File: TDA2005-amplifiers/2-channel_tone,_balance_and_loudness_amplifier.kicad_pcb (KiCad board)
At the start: 2 copper layers, 38 parts, among them U1 TDA2005

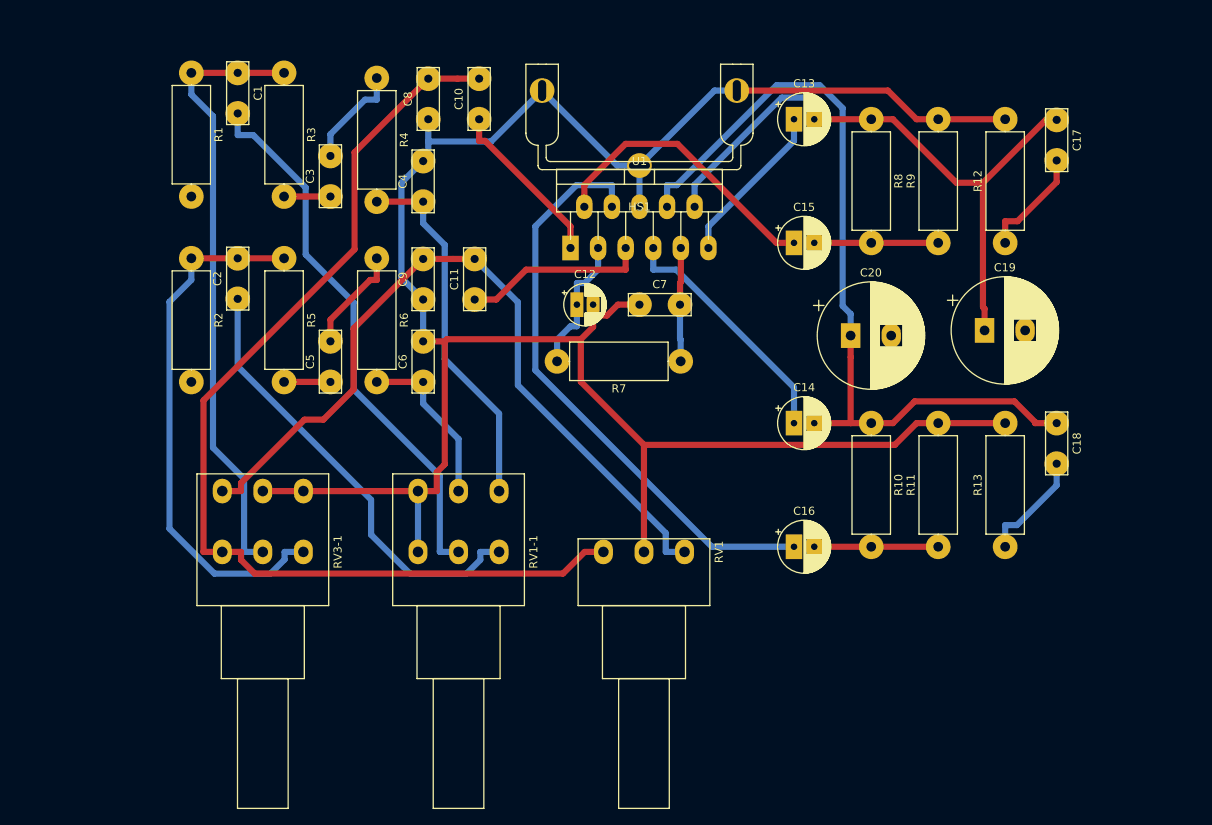
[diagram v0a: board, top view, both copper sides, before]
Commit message: new potentiometers
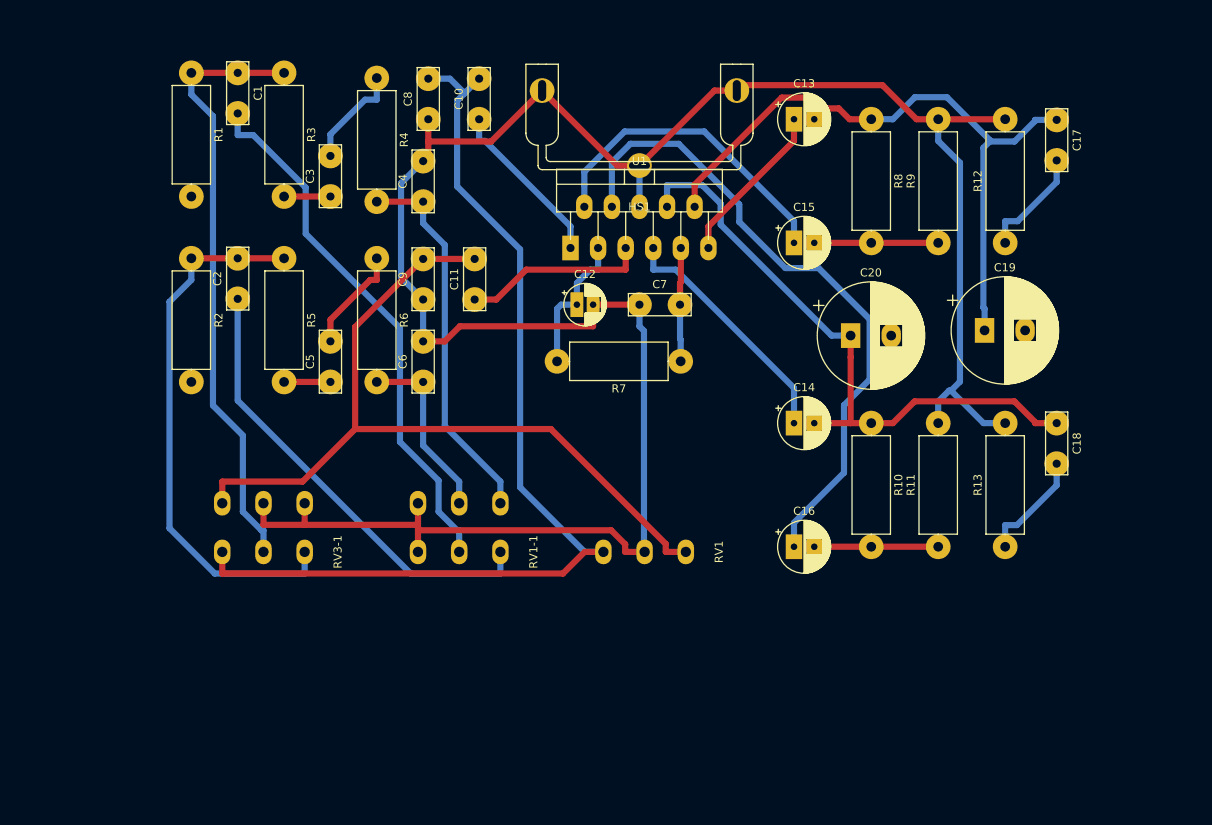
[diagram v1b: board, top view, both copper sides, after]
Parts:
- RV1: footprint My_Misc:Potentiometer_Piher_PC-16_Single_Horizontal_larger -> My_Parts:Potentiometer_single_EK#40910007_10k
- RV1-1, RV3-1: footprint My_Misc:Potentiometer_Piher_PC-16_Dual_Horizontal_larger -> My_Parts:Potentiometer_double_EK#40910227_10k
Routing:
- net Net-(C14-Pad2): track 102.0 -> 77.5 mm
- net GND: track 271.4 -> 287.3 mm
- net Net-(C16-Pad1): track 72.9 -> 80.3 mm
- net Net-(C13-Pad2): track 79.2 -> 83.4 mm
- net Net-(C10-Pad2): track 128.2 -> 124.3 mm
- net Net-(C11-Pad2): track 96.1 -> 100.0 mm
- net Net-(C15-Pad1): track 35.7 -> 39.5 mm
- net Net-(C4-Pad1): track 45.3 -> 46.8 mm
- net Net-(C6-Pad1): track 21.0 -> 22.5 mm
- net Net-(C1-Pad2): track 67.8 -> 66.6 mm
- net Net-(C1-Pad1): track 75.5 -> 74.3 mm
- net Net-(C2-Pad2): track 66.3 -> 67.5 mm
- net Net-(C2-Pad1): track 55.3 -> 56.4 mm
- net Net-(C12-Pad1): track 17.1 -> 17.8 mm

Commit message: new layout
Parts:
- added U2: 4-pole_RL-input_screw_terminal, My_Parts:4-pole_screw_terminal_RL_input, F.Cu at (111.1, 54.6)
- added U3: 2-pole_power_in_screw_terminal, My_Parts:2-pole_power_in_screw_terminal, F.Cu at (111.1, 38.7)
- added U4: 4-pole_RL-output_screw_terminal, My_Parts:4-pole_screw_terminal_RL_output, F.Cu at (240.0, 69.6)
- RV1: footprint My_Parts:Potentiometer_single_EK#40910007_10k -> My_Misc:Potentiometer_Piher_PC-16_Single_Horizontal_larger
- RV1-1, RV3-1: footprint My_Parts:Potentiometer_double_EK#40910227_10k -> My_Misc:Potentiometer_Piher_PC-16_Dual_Horizontal_larger
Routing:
- net GND: track 287.3 -> 428.4 mm
- net +15V: track 14.0 -> 97.5 mm
- net Lout+: track 0.00 -> 33.9 mm
- net Net-(C11-Pad1): track 22.8 -> 41.5 mm, vias 0 -> 1
- net Net-(C10-Pad1): track 21.0 -> 39.5 mm
- net Lin+: track 0.00 -> 17.1 mm
- net Rout+: track 0.00 -> 15.4 mm
- net Rin+: track 0.00 -> 14.9 mm
- net Net-(C14-Pad2): track 77.5 -> 87.6 mm
- net Net-(C1-Pad2): track 66.6 -> 74.3 mm
- net Net-(C13-Pad2): track 83.4 -> 88.9 mm
- net Net-(C13-Pad1): track 20.3 -> 24.6 mm, vias 0 -> 1
- net Net-(C16-Pad1): track 80.3 -> 76.1 mm, vias 0 -> 1
- net Net-(C15-Pad1): track 39.5 -> 36.8 mm
- net Net-(C11-Pad2): track 100.0 -> 97.6 mm
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- added copper zone on B.Cu, net (none)
- added copper zone on B.Cu, net GND
- added copper zone on F.Cu, net GND
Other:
- board outline added: 141.6 x 69.8 mm
- net class 50 added: clearance 0.762, trace_width 1.27, via_dia 2.54, via_drill 0.762

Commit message: kicad6
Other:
- net class 50 removed
- net class Default removed
